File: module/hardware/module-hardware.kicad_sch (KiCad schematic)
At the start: 39 parts, among them J1 USB_B_Micro, J2 40Pin 0.1", J3 Conn_01x02_Male, J4 40Pin 0.1", SW1 SW_Push, U1 NCP1117-3.3_TO252, U2 NCP1117-3.3_TO252, U3 OPA340UA, U4 74LVC2G53, U5 MAX6070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

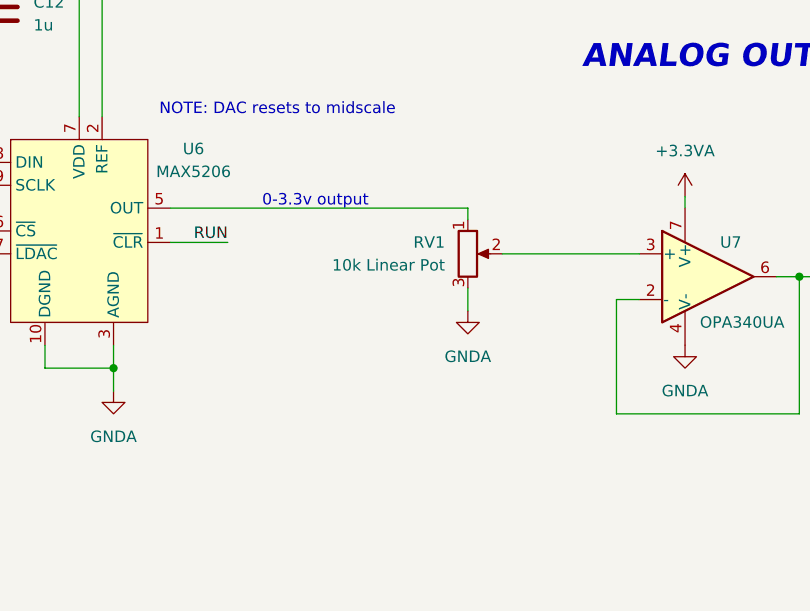
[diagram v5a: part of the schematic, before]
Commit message: Replace slidepot with slidepot daughterboard
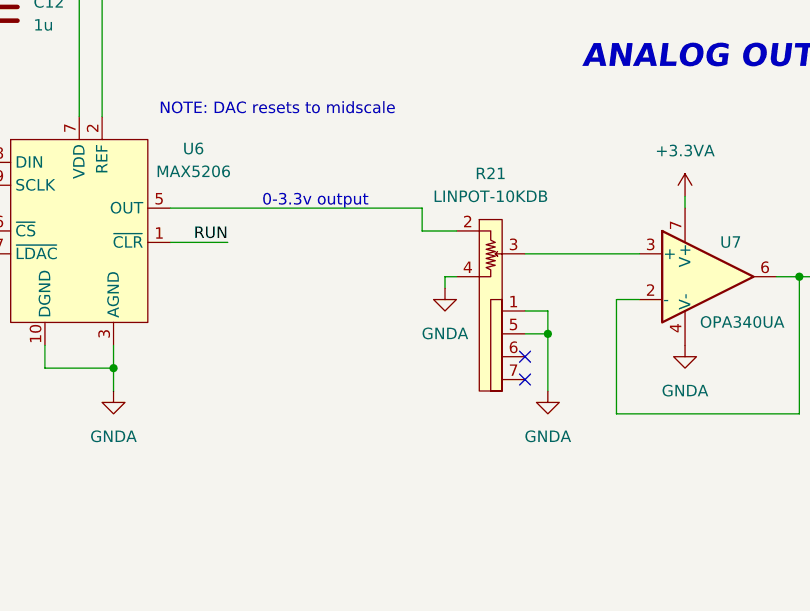
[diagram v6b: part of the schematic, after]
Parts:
- removed RV1: 10k Linear Pot, Potentiometer_THT:Potentiometer_Bourns_PTA6043_Single_Slide, symbol Device:R_Potentiometer
- added R21: LINPOT-10KDB, custom:LINPOT-10KDB, symbol custom-lib:LINPOT-10KDB
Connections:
- net GNDA: now also R21.1, R21.4, R21.5
- net at U6.5 (OUT): now also R21.2
- net at U7.3 (+): now also R21.3
- no-connect marks 3 -> 5
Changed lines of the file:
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@@
   (junction (at 39.37 113.03) (diameter 0) (color 0 0 0 0)
+  )
+  (junction (at 369.57 180.34) (diameter 0) (color 0 0 0 0)
   )
   (junction (at 49.53 52.07) (diameter 0) (color 0 0 0 0)
@@
   (no_connect (at 43.18 128.27))
   (no_connect (at 116.84 128.27))
+  (no_connect (at 367.03 182.88))
+  (no_connect (at 367.03 185.42))
   (no_connect (at 39.37 208.28))
   (wire (pts (xy 29.21 214.63) (xy 29.21 215.9))
@@
     (stroke (width 0) (type default) (color 0 0 0 0))
   )
-  (wire (pts (xy 327.66 166.37) (xy 360.68 166.37))
+  (wire (pts (xy 327.66 166.37) (xy 355.6 166.37))
     (stroke (width 0) (type default) (color 0 0 0 0))
   )
@@
     (stroke (width 0) (type default) (color 0 0 0 0))
   )
+  (wire (pts (xy 367.03 177.8) (xy 369.57 177.8))
+    (stroke (width 0) (type default) (color 0 0 0 0))
+  )
   (wire (pts (xy 113.03 107.95) (xy 113.03 113.03))
     (stroke (width 0) (type default) (color 0 0 0 0))
@@
     (stroke (width 0) (type default) (color 0 0 0 0))
   )
-  (wire (pts (xy 360.68 166.37) (xy 360.68 167.64))
-    (stroke (width 0) (type default) (color 0 0 0 0))
-  )
   (wire (pts (xy 74.93 35.56) (xy 74.93 38.1))
     (stroke (width 0) (type default) (color 0 0 0 0))
@@
     (stroke (width 0) (type default) (color 0 0 0 0))
   )
+  (wire (pts (xy 367.03 171.45) (xy 379.73 171.45))
+    (stroke (width 0) (type default) (color 0 0 0 0))
+  )
   (wire (pts (xy 62.23 49.53) (xy 62.23 52.07))
     (stroke (width 0) (type default) (color 0 0 0 0))
@@
     (stroke (width 0) (type default) (color 0 0 0 0))
   )
+  (wire (pts (xy 358.14 175.26) (xy 358.14 173.99))
+    (stroke (width 0) (type default) (color 0 0 0 0))
+  )
   (wire (pts (xy 133.35 128.27) (xy 133.35 133.35))
     (stroke (width 0) (type default) (color 0 0 0 0))
@@
     (stroke (width 0) (type default) (color 0 0 0 0))
   )
-  (wire (pts (xy 364.49 171.45) (xy 379.73 171.45))
+  (wire (pts (xy 367.03 180.34) (xy 369.57 180.34))
     (stroke (width 0) (type default) (color 0 0 0 0))
   )
@@
     (stroke (width 0) (type default) (color 0 0 0 0))
   )
+  (wire (pts (xy 359.41 168.91) (xy 355.6 168.91))
+    (stroke (width 0) (type default) (color 0 0 0 0))
+  )
   (wire (pts (xy 116.84 125.73) (xy 113.03 125.73))
     (stroke (width 0) (type default) (color 0 0 0 0))
@@
     (stroke (width 0) (type default) (color 0 0 0 0))
   )
+  (wire (pts (xy 358.14 173.99) (xy 359.41 173.99))
+    (stroke (width 0) (type default) (color 0 0 0 0))
+  )
   (wire (pts (xy 59.69 120.65) (xy 55.88 120.65))
     (stroke (width 0) (type default) (color 0 0 0 0))
@@
     (stroke (width 0) (type default) (color 0 0 0 0))
   )
+  (wire (pts (xy 369.57 180.34) (xy 369.57 186.69))
+    (stroke (width 0) (type default) (color 0 0 0 0))
+  )
   (wire (pts (xy 275.59 53.34) (xy 295.91 53.34))
     (stroke (width 0) (type default) (color 0 0 0 0))
@@
     (stroke (width 0) (type default) (color 0 0 0 0))
   )
-  (wire (pts (xy 360.68 175.26) (xy 360.68 177.8))
-    (stroke (width 0) (type default) (color 0 0 0 0))
-  )
   (wire (pts (xy 113.03 102.87) (xy 113.03 107.95))
     (stroke (width 0) (type default) (color 0 0 0 0))
@@
     (stroke (width 0) (type default) (color 0 0 0 0))
   )
+  (wire (pts (xy 355.6 168.91) (xy 355.6 166.37))
+    (stroke (width 0) (type default) (color 0 0 0 0))
+  )
   (wire (pts (xy 228.6 123.19) (xy 227.33 123.19))
     (stroke (width 0) (type default) (color 0 0 0 0))
@@
   )
   (wire (pts (xy 43.18 138.43) (xy 27.94 138.43))
+    (stroke (width 0) (type default) (color 0 0 0 0))
+  )
+  (wire (pts (xy 369.57 177.8) (xy 369.57 180.34))
     (stroke (width 0) (type default) (color 0 0 0 0))
   )
@@
     (pin "1")
   )
+  (symbol (lib_id "custom-lib:LINPOT-10KDB") (at 363.22 176.53 0) (unit 1)
+    (in_bom yes) (on_board yes) (fields_autoplaced)
+    (property "Reference" "R21" (id 0) (at 363.22 162.56 0))
+    (property "Value" "LINPOT-10KDB" (id 1) (at 363.22 165.1 0))
+    (property "Footprint" "custom:LINPOT-10KDB" (id 2) (at 363.22 173.99 0)
+      (effects (font (size 1.27 1.27)) hide)
+    )
+    (property "Datasheet" "" (id 3) (at 363.22 173.99 0)
+      (effects (font (size 1.27 1.27)) hide)
+    )
+    (pin "1")
+    (pin "2")
+    (pin "3")
+    (pin "4")
+    (pin "5")
+    (pin "6")
+    (pin "7")
+  )
   (symbol (lib_id "power:+5VA") (at 283.21 101.6 0) (unit 1)
     (in_bom yes) (on_board yes) (fields_autoplaced)
@@
     (pin "1")
   )
-  (symbol (lib_id "power:GNDA") (at 360.68 177.8 0) (unit 1)
-    (in_bom yes) (on_board yes)
-    (property "Reference" "#PWR040" (id 0) (at 360.68 184.15 0)
-      (effects (font (size 1.27 1.27)) hide)
-    )
-    (property "Value" "GNDA" (id 1) (at 360.68 182.88 0))
-    (property "Footprint" "" (id 2) (at 360.68 177.8 0)
-      (effects (font (size 1.27 1.27)) hide)
-    )
-    (property "Datasheet" "" (id 3) (at 360.68 177.8 0)
+  (symbol (lib_id "power:GNDA") (at 358.14 175.26 0) (unit 1)
+    (in_bom yes) (on_board yes)
+    (property "Reference" "#PWR040" (id 0) (at 358.14 181.61 0)
+      (effects (font (size 1.27 1.27)) hide)
+    )
+    (property "Value" "GNDA" (id 1) (at 358.14 180.34 0))
+    (property "Footprint" "" (id 2) (at 358.14 175.26 0)
+      (effects (font (size 1.27 1.27)) hide)
+    )
+    (property "Datasheet" "" (id 3) (at 358.14 175.26 0)
       (effects (font (size 1.27 1.27)) hide)
     )
@@
     (pin "1")
   )
+  (symbol (lib_id "power:GNDA") (at 369.57 186.69 0) (unit 1)
+    (in_bom yes) (on_board yes)
+    (property "Reference" "#PWR034" (id 0) (at 369.57 193.04 0)
+      (effects (font (size 1.27 1.27)) hide)
+    )
+    (property "Value" "GNDA" (id 1) (at 369.57 191.77 0))
+    (property "Footprint" "" (id 2) (at 369.57 186.69 0)
+      (effects (font (size 1.27 1.27)) hide)
+    )
+    (property "Datasheet" "" (id 3) (at 369.57 186.69 0)
+      (effects (font (size 1.27 1.27)) hide)
+    )
+    (pin "1")
+  )
   (symbol (lib_id "power:+5VD") (at 24.13 33.02 0) (unit 1)
     (in_bom yes) (on_board yes) (fields_autoplaced)
@@
     )
     (pin "1")
-  )
-  (symbol (lib_id "Device:R_Potentiometer") (at 360.68 171.45 0) (unit 1)
-    (in_bom yes) (on_board yes) (fields_autoplaced)
-    (property "Reference" "RV1" (id 0) (at 358.14 170.1799 0)
-      (effects (font (size 1.27 1.27)) (justify right))
-    )
-    (property "Value" "10k Linear Pot" (id 1) (at 358.14 172.7199 0)
-      (effects (font (size 1.27 1.27)) (justify right))
-    )
-    (property "Footprint" "Potentiometer_THT:Potentiometer_Bourns_PTA6043_Single_Slide" (id 2) (at 360.68 171.45 0)
-      (effects (font (size 1.27 1.27)) hide)
-    )
-    (property "Datasheet" "~" (id 3) (at 360.68 171.45 0)
-      (effects (font (size 1.27 1.27)) hide)
-    )
-    (pin "1")
-    (pin "2")
-    (pin "3")
   )
   (symbol (lib_id "Device:R") (at 63.5 110.49 90) (unit 1)
@@
       (reference "#PWR033") (unit 1) (value "GNDD") (footprint "")
     )
+    (path "/81a22314-0e37-4758-8d1a-77bac63d0507"
+      (reference "#PWR034") (unit 1) (value "GNDA") (footprint "")
+    )
     (path "/3a647688-ba1a-4022-91d7-343a5079f3f5"
       (reference "#PWR035") (unit 1) (value "GNDA") (footprint "")
@@
       (reference "R20") (unit 1) (value "10k") (footprint "Resistor_SMD:R_0603_1608Metric_Pad0.98x0.95mm_HandSolder")
     )
-    (path "/b169d545-bdb0-46f0-9e8e-232b739be3d3"
-      (reference "RV1") (unit 1) (value "10k Linear Pot") (footprint "Potentiometer_THT:Potentiometer_Bourns_PTA6043_Single_Slide")
+    (path "/1303cfff-25e2-40b0-b08e-05c3549d45f7"
+      (reference "R21") (unit 1) (value "LINPOT-10KDB") (footprint "custom:LINPOT-10KDB")
     )
     (path "/59c5fdd4-0275-4651-851a-34879fe6317f"

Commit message: Correct direction of input/output connectors for digital signals
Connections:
- net +5VD: now also J2.39 (Pin_39), J4.32 (Pin_32), J4.39 (Pin_39); no longer J2.32 (Pin_32)
- net CBUS_NEXTPRSNT: now also J2.32 (Pin_32); no longer J4.32 (Pin_32)
- net CBUS_SDIN: now also J4.33 (Pin_33); no longer J2.33 (Pin_33)
- net CBUS_SDOUT: now also J2.33 (Pin_33); no longer J4.33 (Pin_33)
- net CBUS_SDRETIN: now also J2.29 (Pin_29); no longer J4.29 (Pin_29)
- net CBUS_SDRETOUT: now also J4.29 (Pin_29); no longer J2.29 (Pin_29)
- net GND: no longer J2.39 (Pin_39), J4.39 (Pin_39)
- net GNDA: now also R21.3; no longer R21.4
- net at U7.3 (+): now also R21.4; no longer R21.3
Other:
- moved on the sheet: R9

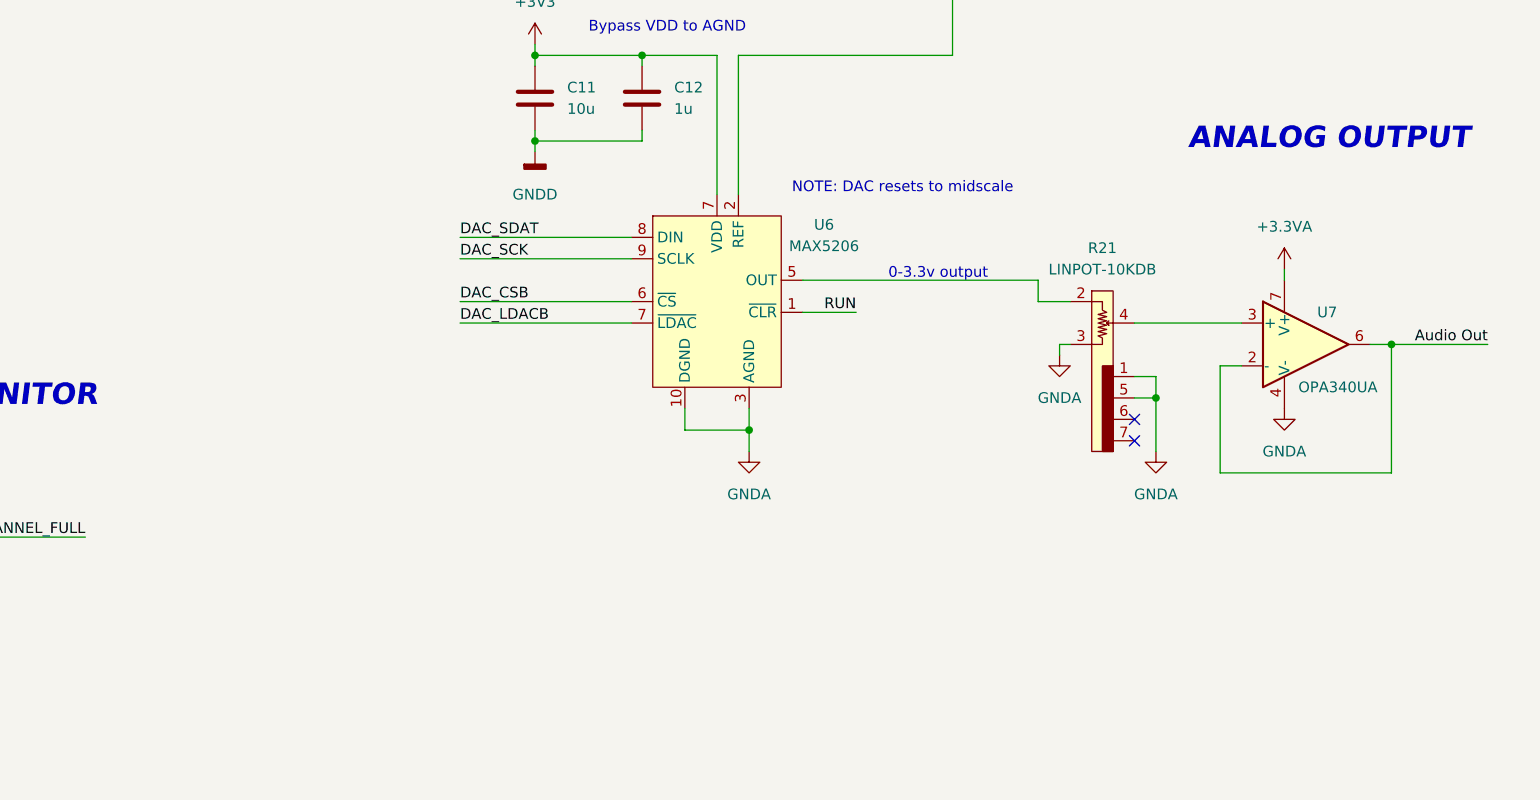
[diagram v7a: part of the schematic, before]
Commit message: Module Analog preliminaty routing complete
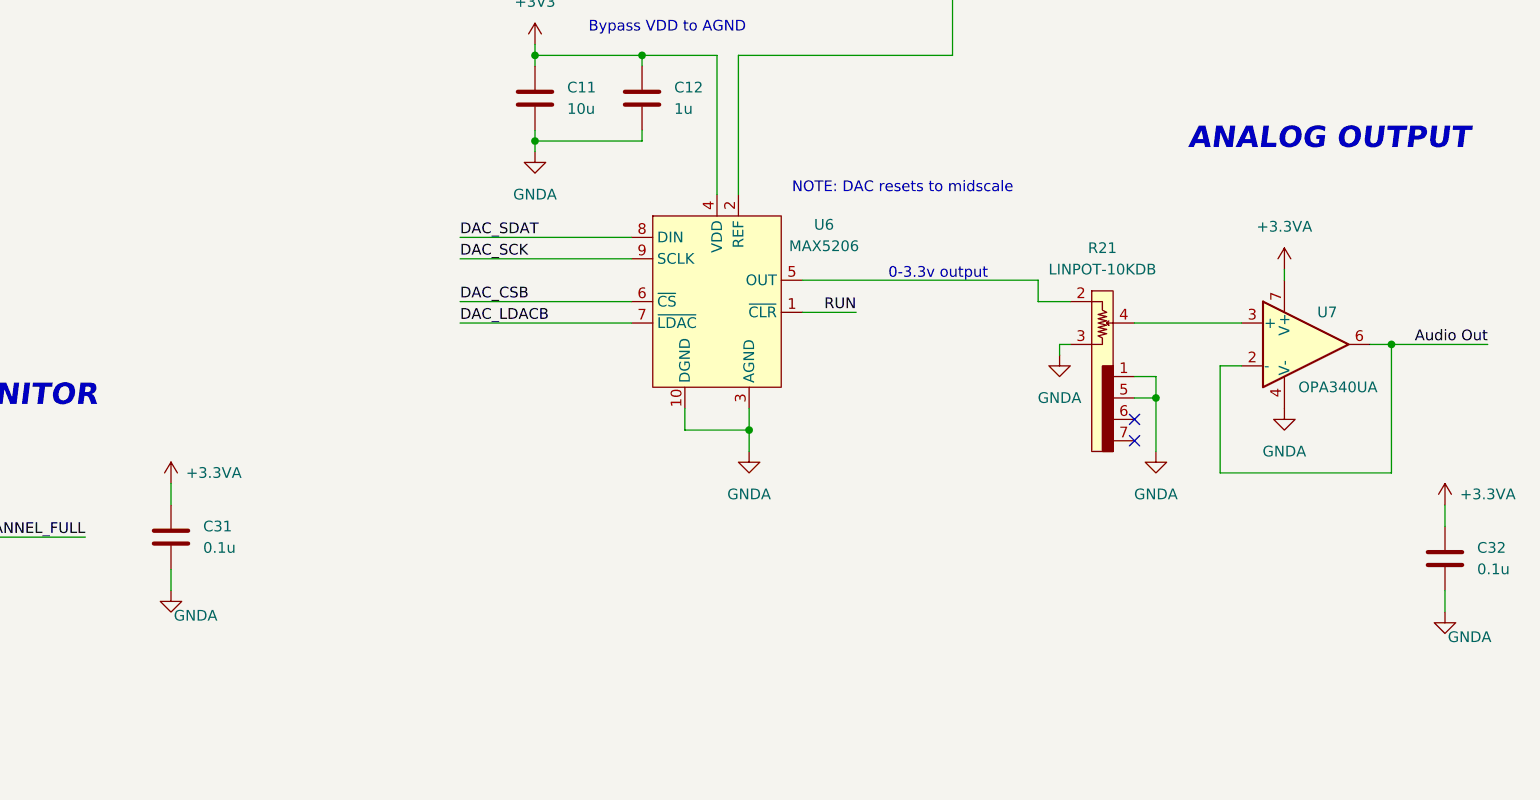
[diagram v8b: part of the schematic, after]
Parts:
- added C31, C32: 0.1u, Capacitor_SMD:C_0603_1608Metric_Pad1.08x0.95mm_HandSolder, symbol Device:C
- J2: footprint Connector_PinSocket_2.54mm:PinSocket_2x20_P2.54mm_Horizontal -> Connector_PinHeader_2.54mm:PinHeader_2x20_P2.54mm_Horizontal
- J4: footprint Connector_PinHeader_2.54mm:PinHeader_2x20_P2.54mm_Horizontal -> Connector_PinSocket_2.54mm:PinSocket_2x20_P2.54mm_Horizontal
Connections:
- net +3.3VA: now also C31.1, C32.1
- net +3V3: now also U6.4 (VDD); no longer U6.7 (~{LDAC})
- net GND: no longer C11.2, C12.2
- net GNDA: now also C11.2, C12.2, C31.2, C32.2
